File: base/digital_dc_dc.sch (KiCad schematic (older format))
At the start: 29 parts, among them U14 AMS1117-5.0, U15 AMS1117-5.0, U17 LM2596S-ADJ

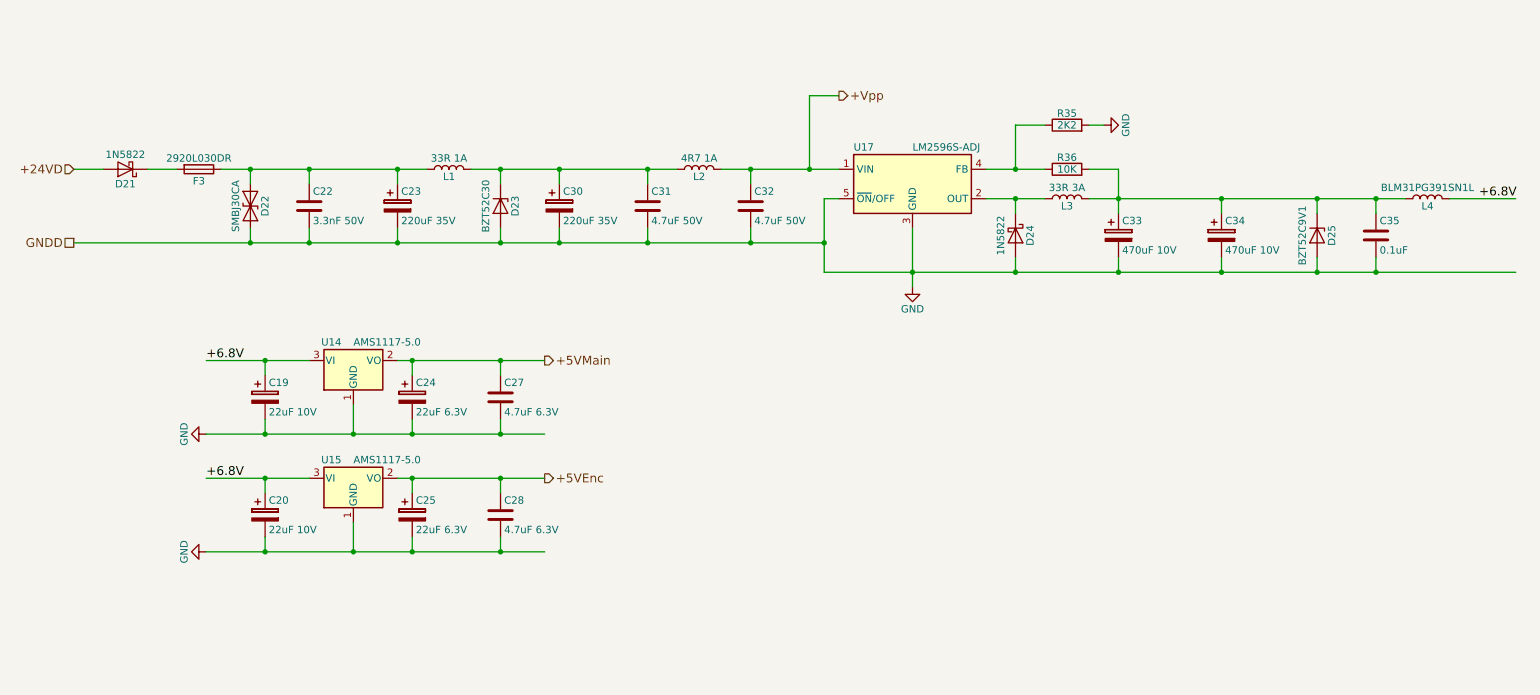
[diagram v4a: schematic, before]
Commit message: some test points
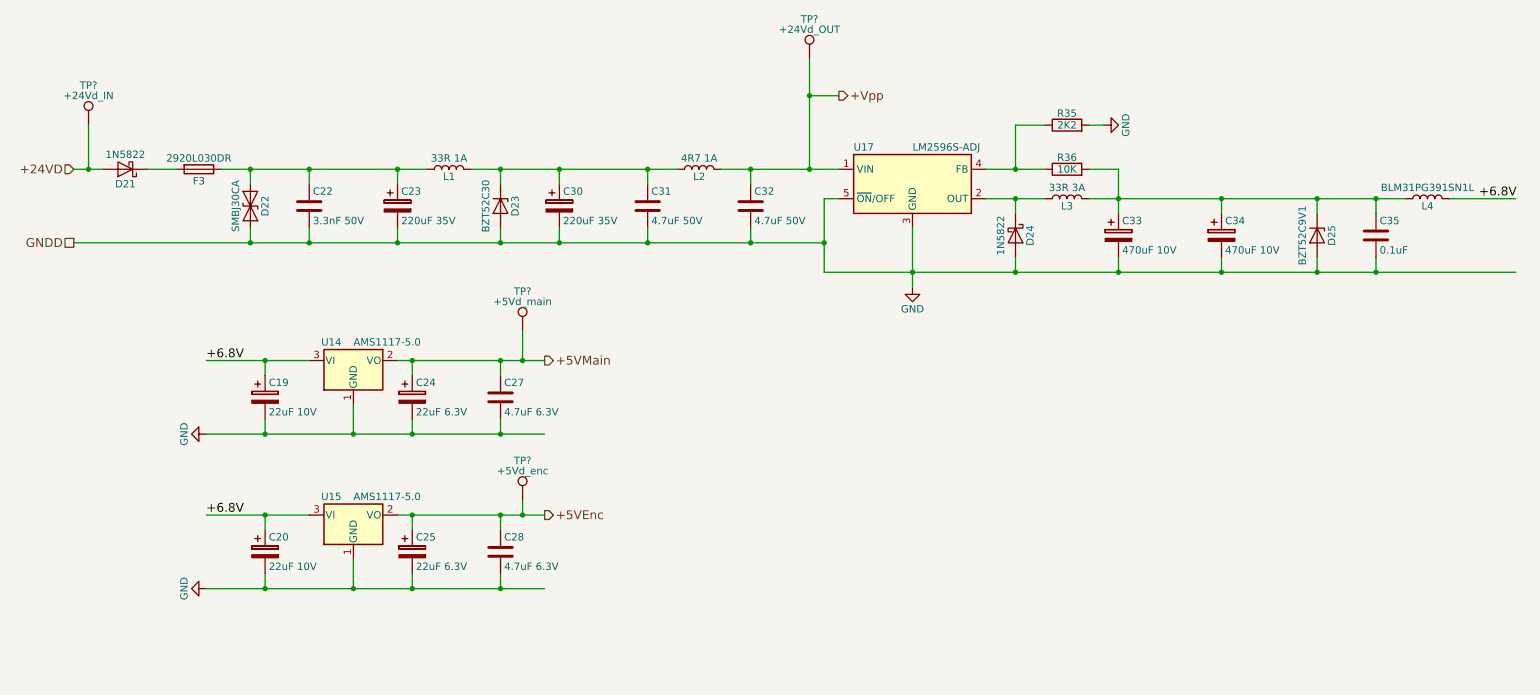
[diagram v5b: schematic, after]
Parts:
- added TP?: +5Vd_main, symbol Test_Point
- added TP?: +5Vd_enc, symbol Test_Point
- added TP?: +24Vd_IN, symbol Test_Point
- added TP?: +24Vd_OUT, symbol Test_Point
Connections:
- wire segments 64 -> 67
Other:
- moved on the sheet: C20, C25, C28, U15
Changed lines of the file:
@@
 Text HLabel 1200 3000 0    60   Input ~ 0
 +24VD
-Text HLabel 4400 5100 2    60   Output ~ 0
+Text HLabel 4400 5350 2    60   Output ~ 0
 +5VEnc
 Text HLabel 4400 4300 2    60   Output ~ 0
@@
 L CP C20
 U 1 1 5A398DF8
-P 2500 5350
-F 0 "C20" H 2525 5450 50  0000 L CNN
-F 1 "22uF 10V" H 2525 5250 50  0000 L CNN
-F 2 "Capacitor_Tantalum_SMD:CP_EIA-3216-18_Kemet-A" H 2538 5200 50  0001 C CNN
-F 3 "" H 2500 5350 50  0001 C CNN
-	1    2500 5350
+P 2500 5600
+F 0 "C20" H 2525 5700 50  0000 L CNN
+F 1 "22uF 10V" H 2525 5500 50  0000 L CNN
+F 2 "Capacitor_Tantalum_SMD:CP_EIA-3216-18_Kemet-A" H 2538 5450 50  0001 C CNN
+F 3 "" H 2500 5600 50  0001 C CNN
+	1    2500 5600
 	1    0    0    -1
 $EndComp
@@
 L AP1117-15 U15
 U 1 1 5A398DFE
-P 3100 5100
-F 0 "U15" H 2950 5225 50  0000 C CNN
-F 1 "AMS1117-5.0" H 3100 5225 50  0000 L CNN
-F 2 "Package_TO_SOT_SMD:SOT-223" H 3100 5300 50  0001 C CNN
-F 3 "" H 3200 4850 50  0001 C CNN
-	1    3100 5100
-	1    0    0    -1
-$EndComp
-Text Label 2100 5100 0    60   ~ 0
+P 3100 5350
+F 0 "U15" H 2950 5475 50  0000 C CNN
+F 1 "AMS1117-5.0" H 3100 5475 50  0000 L CNN
+F 2 "Package_TO_SOT_SMD:SOT-223" H 3100 5550 50  0001 C CNN
+F 3 "" H 3200 5100 50  0001 C CNN
+	1    3100 5350
+	1    0    0    -1
+$EndComp
+Text Label 2100 5350 0    60   ~ 0
 +6.8V
 $Comp
 L GND #PWR023
 U 1 1 5A398E0C
-P 2100 5600
-F 0 "#PWR023" H 2100 5350 50  0001 C CNN
-F 1 "GND" H 2100 5450 50  0000 C CNN
-F 2 "" H 2100 5600 50  0001 C CNN
-F 3 "" H 2100 5600 50  0001 C CNN
-	1    2100 5600
+P 2100 5850
+F 0 "#PWR023" H 2100 5600 50  0001 C CNN
+F 1 "GND" H 2100 5700 50  0000 C CNN
+F 2 "" H 2100 5850 50  0001 C CNN
+F 3 "" H 2100 5850 50  0001 C CNN
+	1    2100 5850
 	0    1    1    0
 $EndComp
@@
 L CP C25
 U 1 1 5A398E13
-P 3500 5350
-F 0 "C25" H 3525 5450 50  0000 L CNN
-F 1 "22uF 6.3V" H 3525 5250 50  0000 L CNN
-F 2 "Capacitor_Tantalum_SMD:CP_EIA-3216-18_Kemet-A" H 3538 5200 50  0001 C CNN
-F 3 "" H 3500 5350 50  0001 C CNN
-	1    3500 5350
+P 3500 5600
+F 0 "C25" H 3525 5700 50  0000 L CNN
+F 1 "22uF 6.3V" H 3525 5500 50  0000 L CNN
+F 2 "Capacitor_Tantalum_SMD:CP_EIA-3216-18_Kemet-A" H 3538 5450 50  0001 C CNN
+F 3 "" H 3500 5600 50  0001 C CNN
+	1    3500 5600
 	1    0    0    -1
 $EndComp
@@
 L C C28
 U 1 1 5A398E1E
-P 4100 5350
-F 0 "C28" H 4125 5450 50  0000 L CNN
-F 1 "4.7uF 6.3V" H 4125 5250 50  0000 L CNN
-F 2 "Capacitor_SMD:C_0603_1608Metric" H 4138 5200 50  0001 C CNN
-F 3 "" H 4100 5350 50  0001 C CNN
-	1    4100 5350
+P 4100 5600
+F 0 "C28" H 4125 5700 50  0000 L CNN
+F 1 "4.7uF 6.3V" H 4125 5500 50  0000 L CNN
+F 2 "Capacitor_SMD:C_0603_1608Metric" H 4138 5450 50  0001 C CNN
+F 3 "" H 4100 5600 50  0001 C CNN
+	1    4100 5600
 	1    0    0    -1
 $EndComp
@@
 Connection ~ 4100 4800
 Wire Wire Line
-	2500 5500 2500 5600
-Wire Wire Line
-	2100 5600 4400 5600
-Wire Wire Line
-	3100 5600 3100 5400
-Connection ~ 2500 5600
-Wire Wire Line
-	2100 5100 2800 5100
-Wire Wire Line
-	2500 5100 2500 5200
-Connection ~ 2500 5100
-Connection ~ 3100 5600
-Wire Wire Line
-	3400 5100 4400 5100
-Wire Wire Line
-	3500 5100 3500 5200
-Wire Wire Line
-	3500 5500 3500 5600
-Connection ~ 3500 5600
-Connection ~ 3500 5100
-Wire Wire Line
-	4100 5200 4100 5100
-Connection ~ 4100 5100
-Wire Wire Line
-	4100 5500 4100 5600
-Connection ~ 4100 5600
+	2500 5750 2500 5850
+Wire Wire Line
+	2100 5850 4400 5850
+Wire Wire Line
+	3100 5850 3100 5650
+Connection ~ 2500 5850
+Wire Wire Line
+	2100 5350 2800 5350
+Wire Wire Line
+	2500 5350 2500 5450
+Connection ~ 2500 5350
+Connection ~ 3100 5850
+Wire Wire Line
+	3400 5350 4400 5350
+Wire Wire Line
+	3500 5350 3500 5450
+Wire Wire Line
+	3500 5750 3500 5850
+Connection ~ 3500 5850
+Connection ~ 3500 5350
+Wire Wire Line
+	4100 5450 4100 5350
+Connection ~ 4100 5350
+Wire Wire Line
+	4100 5750 4100 5850
+Connection ~ 4100 5850
 Wire Wire Line
 	9000 3700 9000 3600
@@
 Connection ~ 10050 3700
 Wire Wire Line
-	6200 3000 6200 2500
+	6200 2250 6200 3000
 Wire Wire Line
 	6200 2500 6400 2500
 Connection ~ 6200 3000
+$Comp
+L Test_Point TP?
+U 1 1 5A49ED26
+P 4250 4100
+F 0 "TP?" H 4250 4370 50  0000 C CNN
+F 1 "+5Vd_main" H 4250 4300 50  0000 C CNN
+F 2 "" H 4450 4100 50  0001 C CNN
+F 3 "" H 4450 4100 50  0001 C CNN
+	1    4250 4100
+	1    0    0    -1
+$EndComp
+Wire Wire Line
+	4250 4100 4250 4300
+Connection ~ 4250 4300
+$Comp
+L Test_Point TP?
+U 1 1 5A49EF64
+P 4250 5250
+F 0 "TP?" H 4250 5520 50  0000 C CNN
+F 1 "+5Vd_enc" H 4250 5450 50  0000 C CNN
+F 2 "" H 4450 5250 50  0001 C CNN
+F 3 "" H 4450 5250 50  0001 C CNN
+	1    4250 5250
+	1    0    0    -1
+$EndComp
+Wire Wire Line
+	4250 5250 4250 5350
+Connection ~ 4250 5350
+$Comp
+L Test_Point TP?
+U 1 1 5A4A0D23
+P 1300 2700
+F 0 "TP?" H 1300 2970 50  0000 C CNN
+F 1 "+24Vd_IN" H 1300 2900 50  0000 C CNN
+F 2 "" H 1500 2700 50  0001 C CNN
+F 3 "" H 1500 2700 50  0001 C CNN
+	1    1300 2700
+	1    0    0    -1
+$EndComp
+Wire Wire Line
+	1300 2700 1300 3000
+Connection ~ 1300 3000
+$Comp
+L Test_Point TP?
+U 1 1 5A4A0FEB
+P 6200 2250
+F 0 "TP?" H 6200 2520 50  0000 C CNN
+F 1 "+24Vd_OUT" H 6200 2450 50  0000 C CNN
+F 2 "" H 6400 2250 50  0001 C CNN
+F 3 "" H 6400 2250 50  0001 C CNN
+	1    6200 2250
+	1    0    0    -1
+$EndComp
+Connection ~ 6200 2500
 $EndSCHEMATC

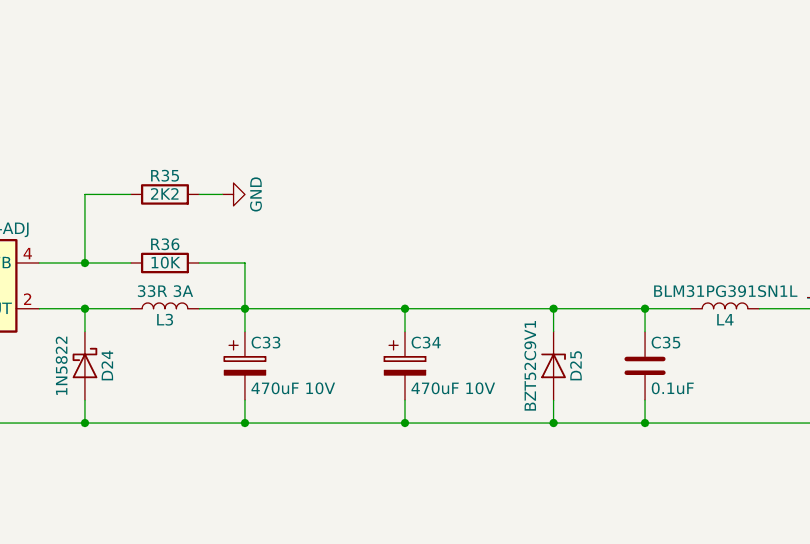
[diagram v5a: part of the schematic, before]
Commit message: A few updates to test points.
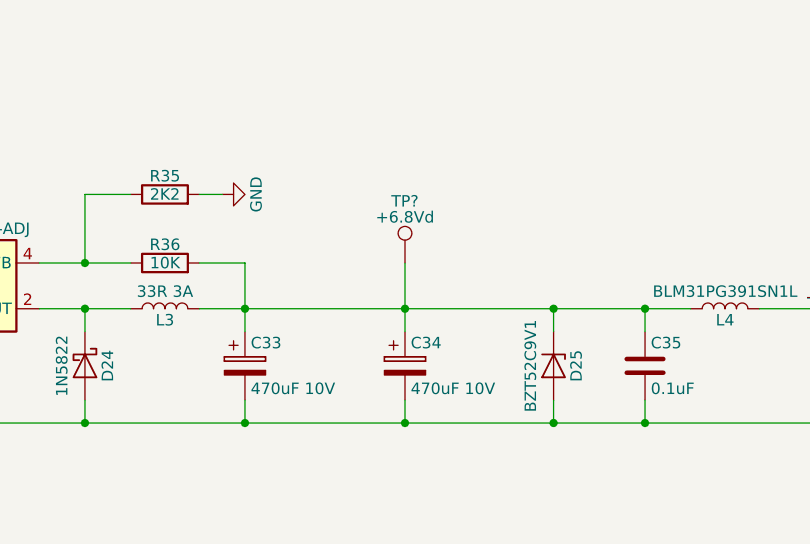
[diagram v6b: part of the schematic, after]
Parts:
- added TP?: +6.8Vd, symbol Test_Point
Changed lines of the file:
@@
 	9000 3700 9000 3600
 Wire Wire Line
-	9000 3300 9000 3200
+	9000 3000 9000 3300
 Connection ~ 9000 3200
 Connection ~ 10050 3700
@@
 $EndComp
 Connection ~ 6200 2500
+$Comp
+L Test_Point TP?
+U 1 1 5A456659
+P 9000 3000
+F 0 "TP?" H 9000 3270 50  0000 C CNN
+F 1 "+6.8Vd" H 9000 3200 50  0000 C CNN
+F 2 "" H 9200 3000 50  0001 C CNN
+F 3 "" H 9200 3000 50  0001 C CNN
+	1    9000 3000
+	1    0    0    -1
+$EndComp
 $EndSCHEMATC
